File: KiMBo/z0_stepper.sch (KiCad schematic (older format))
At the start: 25 parts

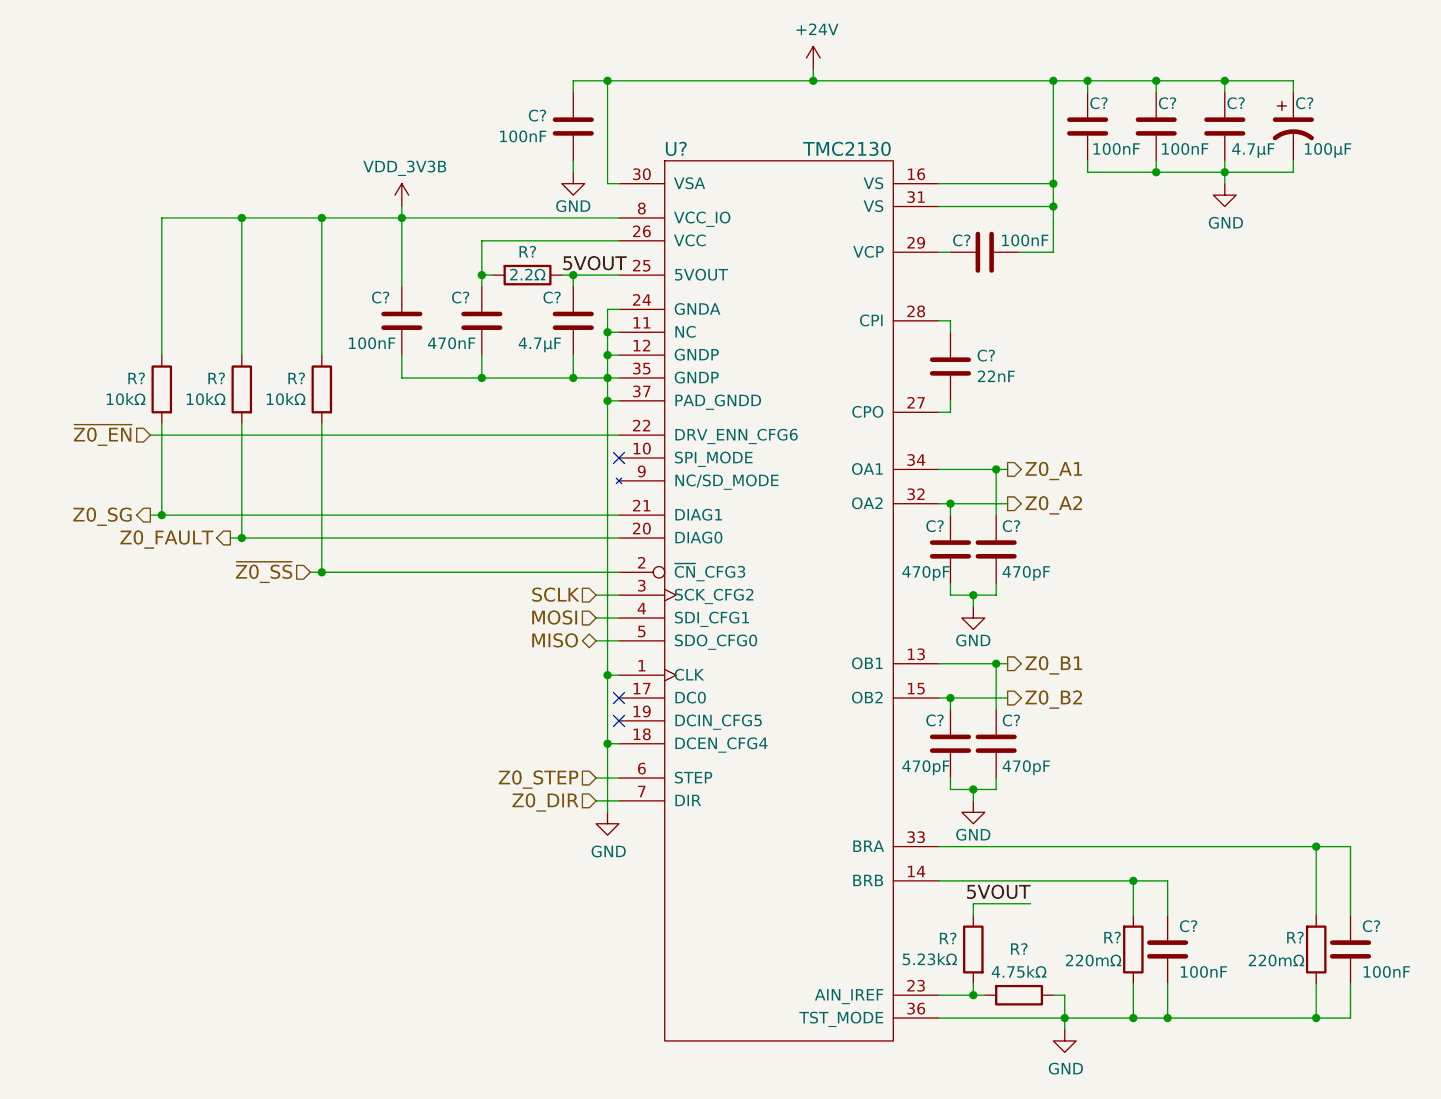
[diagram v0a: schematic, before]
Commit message: Annotate all components, now passing ERC, added ferrites to the rest of the connectors
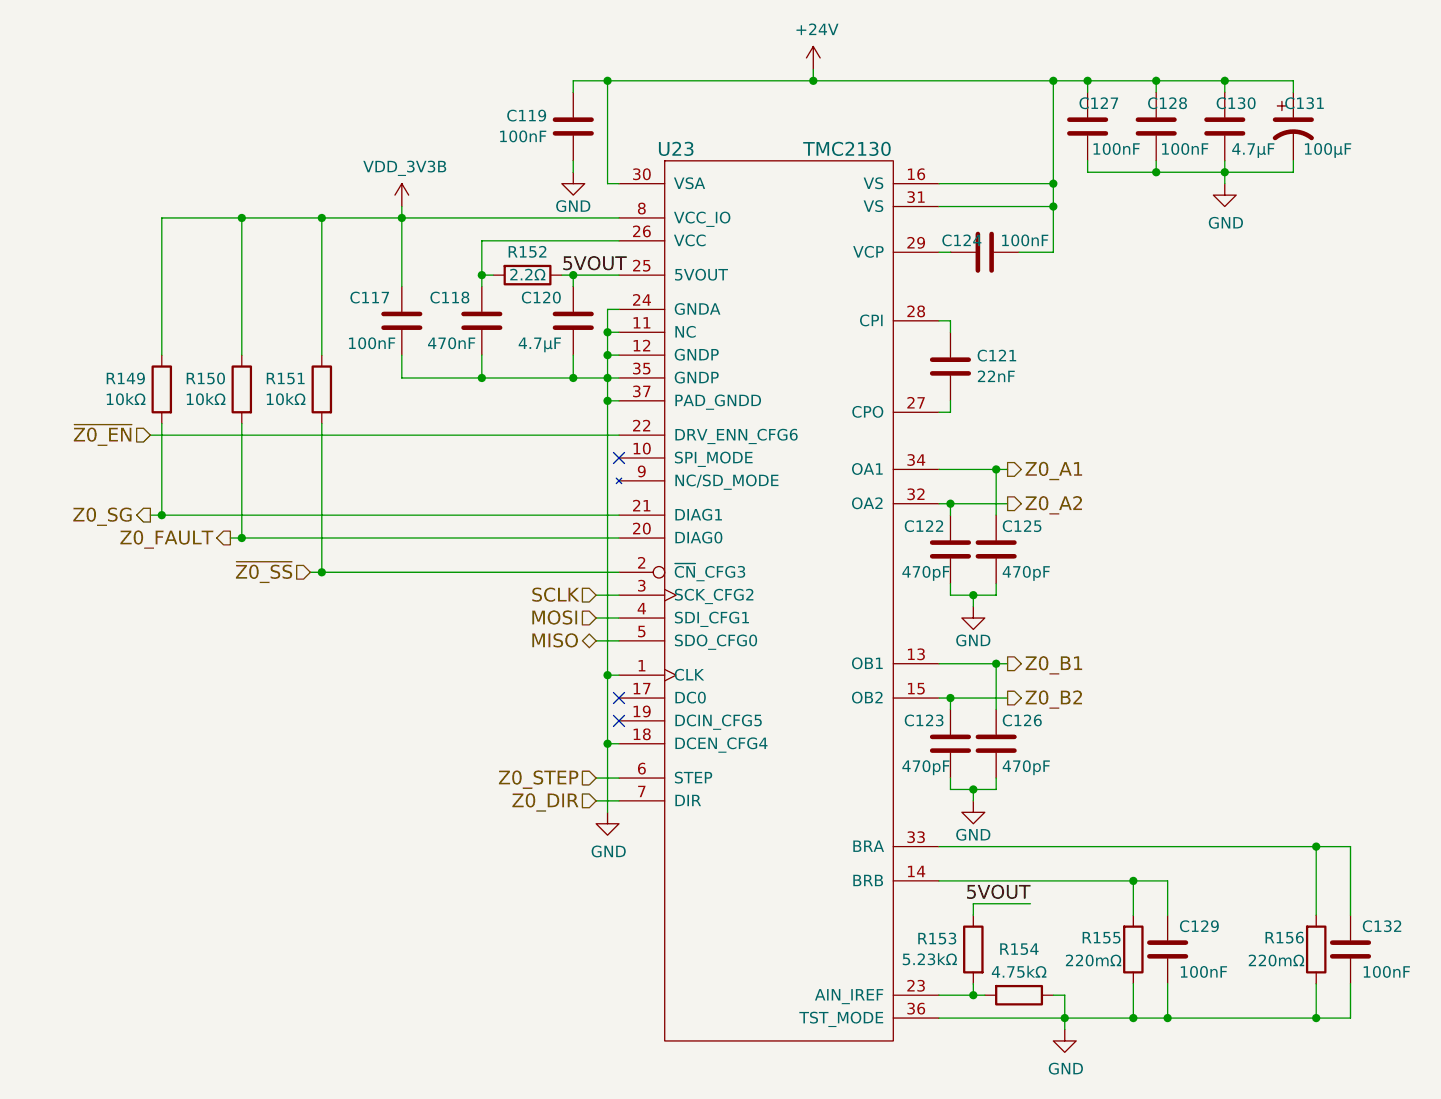
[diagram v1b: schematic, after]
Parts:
- gave numbers to parts that had none: 25

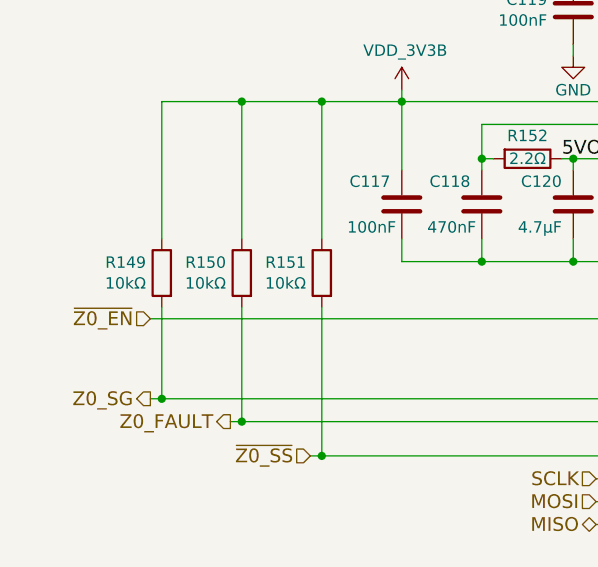
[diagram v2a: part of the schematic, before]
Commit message: Reorder the SS and EN lines from the shift registers such that the previously enabled/disabled motors stay enabled/disabled whilst writting to the shift register
Change 10k resistors to 4.7k, flip the open-drain inverter connected to B15 (PMTC_PGOOD)

Update the links in the README

Update the PDF schematic
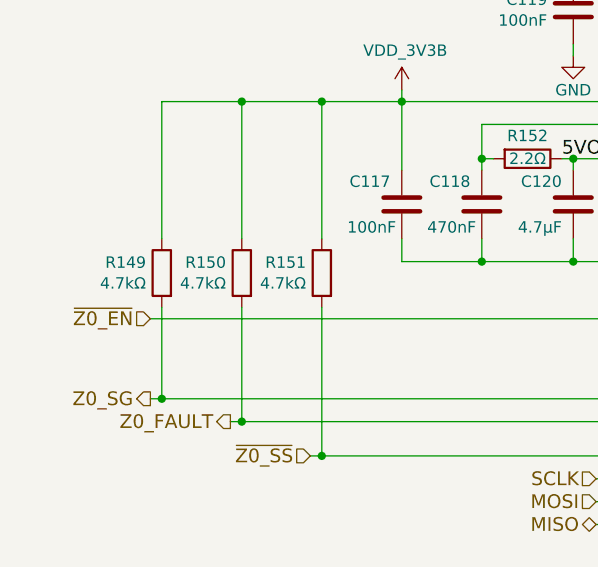
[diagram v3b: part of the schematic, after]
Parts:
- R149, R150, R151: value 10kΩ -> 4.7kΩ
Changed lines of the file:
@@
 F 0 "C119" H 6986 3104 50  0000 R CNN
 F 1 "100nF" H 6986 3195 50  0000 R CNN
-F 2 "" H 7138 3000 50  0000 C CNN
+F 2 "" H 7138 3000 50  0001 C CNN
 F 3 "" H 7100 3150 50  0000 C CNN
 	1    7100 3150
@@
 F 0 "C124" V 8850 3600 50  0000 C CNN
 F 1 "100nF" V 8850 3875 50  0000 C CNN
-F 2 "" H 8938 3550 50  0000 C CNN
+F 2 "" H 8938 3550 50  0001 C CNN
 F 3 "" H 8900 3700 50  0000 C CNN
 	1    8900 3700
@@
 F 0 "C131" H 10300 3250 50  0000 C CNN
 F 1 "100μF" H 10400 3050 50  0000 C CNN
-F 2 "" H 10250 3150 50  0000 C CNN
+F 2 "" H 10250 3150 50  0001 C CNN
 F 3 "" H 10250 3150 50  0000 C CNN
 	1    10250 3150
@@
 F 0 "C127" H 9300 3250 50  0000 C CNN
 F 1 "100nF" H 9225 3050 50  0000 C CNN
-F 2 "" H 9388 3000 50  0000 C CNN
+F 2 "" H 9388 3000 50  0001 C CNN
 F 3 "" H 9350 3150 50  0000 C CNN
 	1    9350 3150
@@
 F 0 "C128" H 9600 3250 50  0000 C CNN
 F 1 "100nF" H 9525 3050 50  0000 C CNN
-F 2 "" H 9688 3000 50  0000 C CNN
+F 2 "" H 9688 3000 50  0001 C CNN
 F 3 "" H 9650 3150 50  0000 C CNN
 	1    9650 3150
@@
 F 0 "C121" H 8865 4246 50  0000 L CNN
 F 1 "22nF" H 8865 4155 50  0000 L CNN
-F 2 "" H 8788 4050 50  0000 C CNN
+F 2 "" H 8788 4050 50  0001 C CNN
 F 3 "" H 8750 4200 50  0000 C CNN
 	1    8750 4200
@@
 F 0 "R156" H 10300 6700 50  0000 R CNN
 F 1 "220mΩ" H 10300 6800 50  0000 R CNN
-F 2 "" V 10280 6750 50  0000 C CNN
+F 2 "" V 10280 6750 50  0001 C CNN
 F 3 "" H 10350 6750 50  0000 C CNN
 	1    10350 6750
@@
 F 0 "R155" H 9500 6700 50  0000 R CNN
 F 1 "220mΩ" H 9500 6800 50  0000 R CNN
-F 2 "" V 9480 6750 50  0000 C CNN
+F 2 "" V 9480 6750 50  0001 C CNN
 F 3 "" H 9550 6750 50  0000 C CNN
 	1    9550 6750
@@
 F 0 "R152" V 6800 3800 50  0000 C CNN
 F 1 "2.2Ω" V 6900 3800 50  0000 C CNN
-F 2 "" V 6830 3800 50  0000 C CNN
+F 2 "" V 6830 3800 50  0001 C CNN
 F 3 "" H 6900 3800 50  0000 C CNN
 	1    6900 3800
@@
 F 0 "C118" H 6750 4100 50  0000 L CNN
 F 1 "470nF" H 6725 3900 50  0000 L CNN
-F 2 "" H 6738 3850 50  0000 C CNN
+F 2 "" H 6738 3850 50  0001 C CNN
 F 3 "" H 6700 4000 50  0000 C CNN
 	1    6700 4000
@@
 F 0 "C129" H 9750 6850 50  0000 L CNN
 F 1 "100nF" H 9750 6650 50  0000 L CNN
-F 2 "" H 9738 6600 50  0000 C CNN
+F 2 "" H 9738 6600 50  0001 C CNN
 F 3 "" H 9700 6750 50  0000 C CNN
 	1    9700 6750
@@
 P 5650 4300
 F 0 "R150" H 5719 4346 50  0000 L CNN
-F 1 "10kΩ" H 5719 4255 50  0000 L CNN
-F 2 "" V 5580 4300 50  0000 C CNN
+F 1 "4.7kΩ" H 5719 4255 50  0000 L CNN
+F 2 "" V 5580 4300 50  0001 C CNN
 F 3 "" H 5650 4300 50  0000 C CNN
 	1    5650 4300
@@
 F 0 "C120" H 7150 4100 50  0000 L CNN
 F 1 "4.7μF" H 7150 3900 50  0000 L CNN
-F 2 "" H 7138 3850 50  0000 C CNN
+F 2 "" H 7138 3850 50  0001 C CNN
 F 3 "" H 7100 4000 50  0000 C CNN
 	1    7100 4000
@@
 F 0 "R153" H 8919 6796 50  0000 L CNN
 F 1 "5.23kΩ" H 8919 6705 50  0000 L CNN
-F 2 "" V 8780 6750 50  0000 C CNN
+F 2 "" V 8780 6750 50  0001 C CNN
 F 3 "" H 8850 6750 50  0000 C CNN
 	1    8850 6750
@@
 F 0 "R154" V 8850 6950 50  0000 C CNN
 F 1 "4.75kΩ" V 8950 6950 50  0000 C CNN
-F 2 "" V 8980 6950 50  0000 C CNN
+F 2 "" V 8980 6950 50  0001 C CNN
 F 3 "" H 9050 6950 50  0000 C CNN
 	1    9050 6950
@@
 P 6000 4300
 F 0 "R151" H 6069 4346 50  0000 L CNN
-F 1 "10kΩ" H 6069 4255 50  0000 L CNN
-F 2 "" V 5930 4300 50  0000 C CNN
+F 1 "4.7kΩ" H 6069 4255 50  0000 L CNN
+F 2 "" V 5930 4300 50  0001 C CNN
 F 3 "" H 6000 4300 50  0000 C CNN
 	1    6000 4300
@@
 F 0 "C132" H 10550 6850 50  0000 L CNN
 F 1 "100nF" H 10550 6650 50  0000 L CNN
-F 2 "" H 10538 6600 50  0000 C CNN
+F 2 "" H 10538 6600 50  0001 C CNN
 F 3 "" H 10500 6750 50  0000 C CNN
 	1    10500 6750
@@
 F 0 "C122" H 8775 5100 50  0000 L CNN
 F 1 "470pF" H 8750 4900 50  0000 L CNN
-F 2 "" H 8788 4850 50  0000 C CNN
+F 2 "" H 8788 4850 50  0001 C CNN
 F 3 "" H 8750 5000 50  0000 C CNN
 	1    8750 5000
@@
 F 0 "C125" H 8975 5100 50  0000 L CNN
 F 1 "470pF" H 8975 4900 50  0000 L CNN
-F 2 "" H 8988 4850 50  0000 C CNN
+F 2 "" H 8988 4850 50  0001 C CNN
 F 3 "" H 8950 5000 50  0000 C CNN
 	1    8950 5000
@@
 F 0 "C123" H 8775 5950 50  0000 L CNN
 F 1 "470pF" H 8750 5750 50  0000 L CNN
-F 2 "" H 8788 5700 50  0000 C CNN
+F 2 "" H 8788 5700 50  0001 C CNN
 F 3 "" H 8750 5850 50  0000 C CNN
 	1    8750 5850
@@
 F 0 "C126" H 8975 5950 50  0000 L CNN
 F 1 "470pF" H 8975 5750 50  0000 L CNN
-F 2 "" H 8988 5700 50  0000 C CNN
+F 2 "" H 8988 5700 50  0001 C CNN
 F 3 "" H 8950 5850 50  0000 C CNN
 	1    8950 5850
@@
 F 0 "U23" H 7550 6250 60  0000 C CNN
 F 1 "TMC2130" H 8300 6250 60  0000 C CNN
-F 2 "" H 8000 5050 60  0000 C CNN
+F 2 "" H 8000 5050 60  0001 C CNN
 F 3 "" H 8000 5050 60  0000 C CNN
 	1    8000 4750
@@
 P 5300 4300
 F 0 "R149" H 5369 4346 50  0000 L CNN
-F 1 "10kΩ" H 5369 4255 50  0000 L CNN
-F 2 "" V 5230 4300 50  0000 C CNN
+F 1 "4.7kΩ" H 5369 4255 50  0000 L CNN
+F 2 "" V 5230 4300 50  0001 C CNN
 F 3 "" H 5300 4300 50  0000 C CNN
 	1    5300 4300
@@
 F 0 "C130" H 9900 3250 50  0000 C CNN
 F 1 "4.7μF" H 9825 3050 50  0000 C CNN
-F 2 "" H 9988 3000 50  0000 C CNN
+F 2 "" H 9988 3000 50  0001 C CNN
 F 3 "" H 9950 3150 50  0000 C CNN
 	1    9950 3150
@@
 F 0 "C117" H 6400 4100 50  0000 L CNN
 F 1 "100nF" H 6375 3900 50  0000 L CNN
-F 2 "" H 6388 3850 50  0000 C CNN
+F 2 "" H 6388 3850 50  0001 C CNN
 F 3 "" H 6350 4000 50  0000 C CNN
 	1    6350 4000
